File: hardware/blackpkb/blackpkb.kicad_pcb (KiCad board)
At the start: 2 copper layers, 96 x 96 mm, 32 parts, among them SW1 SW_Push_45deg, SW10 SW_Push_45deg, SW11 SW_Push_45deg, SW12 SW_Push_45deg, SW13 RotaryEncoder_Switch, SW2 SW_Push_45deg, SW3 SW_Push_45deg, SW4 SW_Push_45deg, SW5 SW_Push_45deg, SW6 SW_Push_45deg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

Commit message: hardware v0.2
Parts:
- removed D10, D11, D12: 1N4148, Diode_THT:D_DO-35_SOD27_P7.62mm_Horizontal
- removed SW10, SW11, SW12, SW4, SW8, SW9: SW_Push_45deg, Button_Switch_Keyboard:SW_Cherry_MX_1.00u_PCB
- added R1: 330, Resistor_THT:R_Axial_DIN0207_L6.3mm_D2.5mm_P7.62mm_Horizontal, F.Cu at (202.1, 64.2)
- added R2: 330, Resistor_THT:R_Axial_DIN0207_L6.3mm_D2.5mm_P7.62mm_Horizontal, F.Cu at (202.0, 75.0)
- added R3: 330, Resistor_THT:R_Axial_DIN0207_L6.3mm_D2.5mm_P7.62mm_Horizontal, F.Cu at (202.0, 85.7)
- D4, D8, D9: value 1N4148 -> LED_Small; footprint Diode_THT:D_DO-35_SOD27_P7.62mm_Horizontal -> LED_THT:LED_D3.0mm
- moved D9 53.2 mm to (207.1, 79.7), turned to -90 degrees
- moved G*** 45.6 mm to (171.2, 35.6)
- moved H4 25.0 mm to (210.0, 90.0)
- moved H3 20.0 mm to (135.0, 90.0)
- moved D8 17.2 mm to (207.2, 69.2), turned to -90 degrees
- moved G*** 15.6 mm to (205.8, 50.1)
- moved H2 15.0 mm to (210.0, 20.0)
- moved D4 11.2 mm to (207.2, 58.2), turned to -90 degrees
- moved U1 6.29 mm to (136.3, 43.6)
- moved SW13 3.57 mm to (198.6, 43.0)
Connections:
- D4 pad 1: /ROW_1 -> /LED_YELLOW
- D8 pad 1: /ROW_2 -> /LED_GREEN
- D9 pad 1: /ROW_3 -> /LED_RED
- U1 pad 13: /ROW_3 -> unconnected-(U1-PB5-Pad13)
- U1 pad 20: unconnected-(U1-3V3-Pad20) -> +3.3V
- U1 pad 26: unconnected-(U1-PA0-Pad26) -> /LED_RED
- U1 pad 27: unconnected-(U1-PA1-Pad27) -> /LED_GREEN
- U1 pad 28: unconnected-(U1-PA2-Pad28) -> /LED_YELLOW
- U1 pad 4: /COL_4 -> unconnected-(U1-PB15-Pad4)
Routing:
- net /ROW_3: track 165.1 -> 0.00 mm
- net /COL_4: track 105.1 -> 0.00 mm
- net /LED_RED: track 0.00 -> 84.0 mm
- net /LED_GREEN: track 0.00 -> 81.1 mm
- net /LED_YELLOW: track 0.00 -> 77.6 mm
- net /ROW_1: track 127.2 -> 60.3 mm
- net /ROW_2: track 146.2 -> 82.0 mm, vias 0 -> 2
- net +3.3V: track 0.00 -> 54.2 mm
- net /ENCODER_B: track 55.7 -> 73.2 mm, vias 0 -> 2
- net /COL_3: track 87.9 -> 72.5 mm
- net /COL_2: track 70.7 -> 55.9 mm
- net /COL_1: track 53.3 -> 39.4 mm
- net Net-(D12-A): track 13.5 -> 0.00 mm
- net Net-(D10-A): track 13.4 -> 0.00 mm
- net Net-(D11-A): track 13.3 -> 0.00 mm
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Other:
- board size 96 x 96 mm -> 81 x 76 mm
- board text added: "bluepkb 07/24 - v0.2 alcato"
- board text removed: "author - alcato"
- board text removed: "bluepkb"
- board text removed: "v0.1"

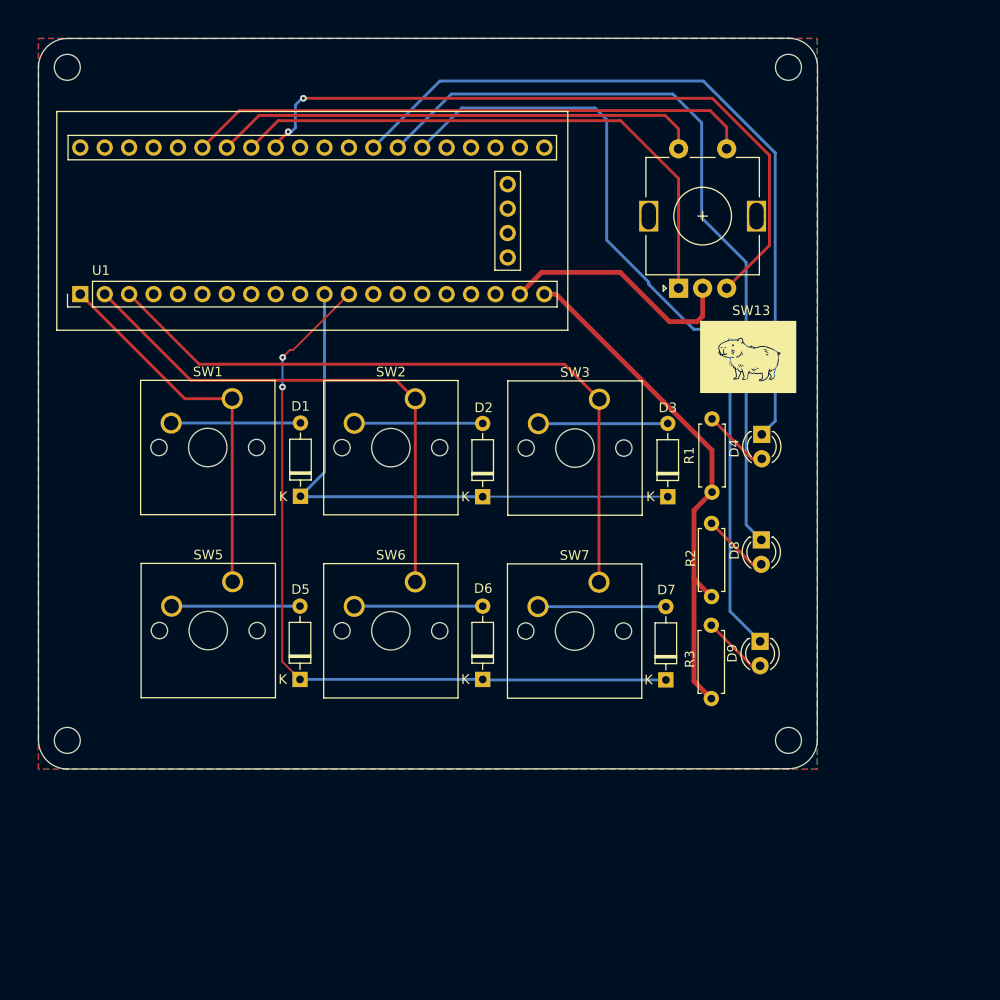
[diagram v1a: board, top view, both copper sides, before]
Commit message: the keyboard now works. Can use one key to type number 1 :>
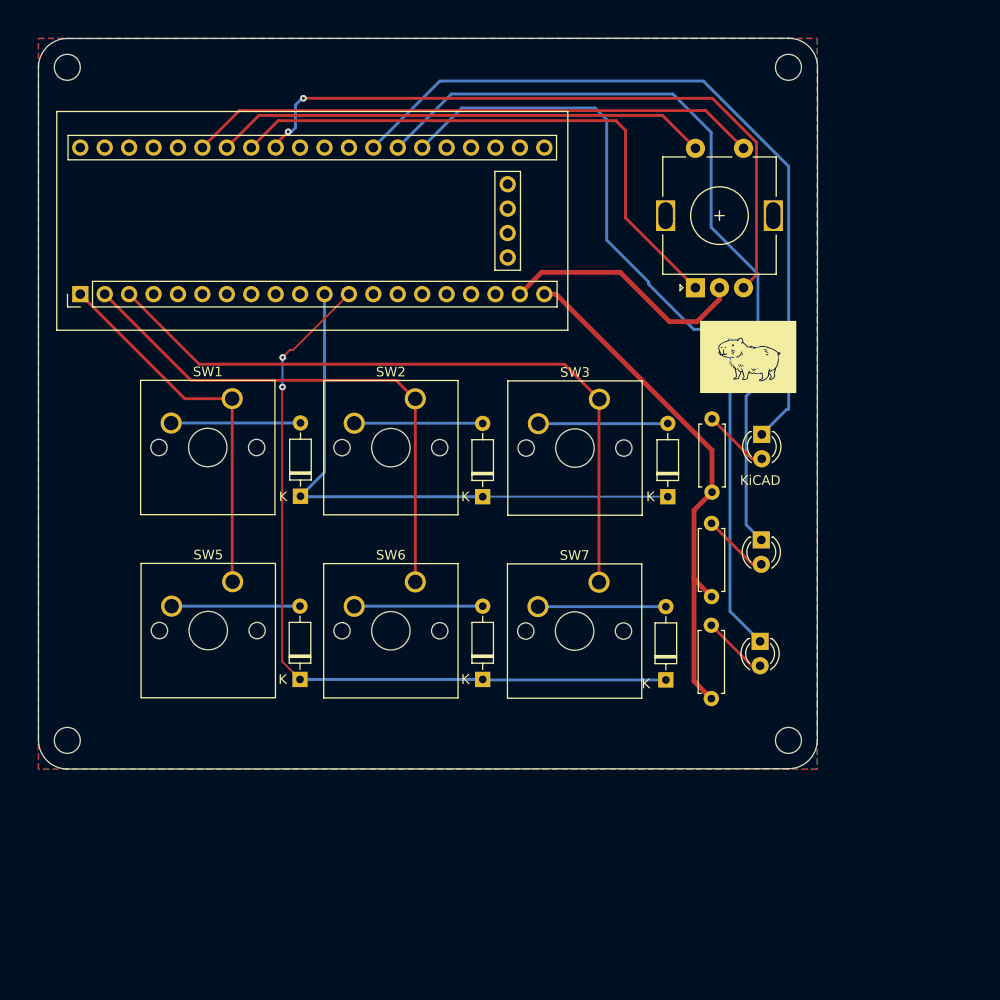
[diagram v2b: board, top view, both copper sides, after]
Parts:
- moved SW13 1.75 mm to (200.3, 42.9)
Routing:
- net /ENCODER_B: track 73.2 -> 71.3 mm
- net /LED_YELLOW: track 77.6 -> 78.9 mm
- net /LED_GREEN: track 81.1 -> 82.1 mm
- net /GND: track 25.2 -> 26.0 mm
- net /ENCODER_S2: track 51.0 -> 51.5 mm
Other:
- board text added: "K"
- board text added: "KiCAD"
- board text added: "bluepkb 07/24 - v0.3 alcato"
- board text removed: "bluepkb 07/24 - v0.2 alcato"
